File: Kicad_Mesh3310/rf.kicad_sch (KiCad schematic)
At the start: 34 parts, among them U1 TPE4259-63, U10 SX1262IMLTRT, X1 S201632M10PF10PPM 32MHz

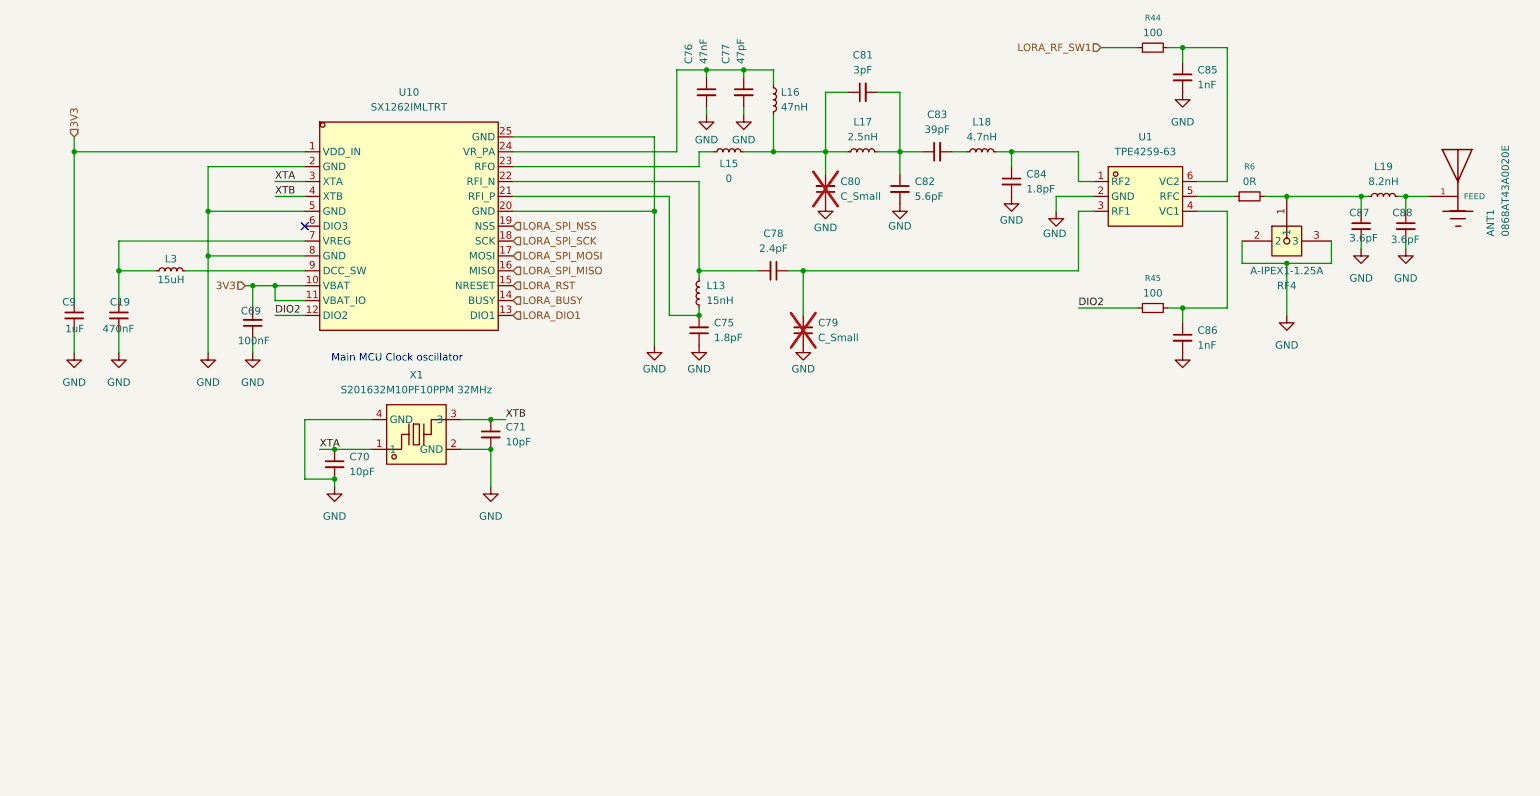
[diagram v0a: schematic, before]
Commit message: shematic changes
small changes in NRF component
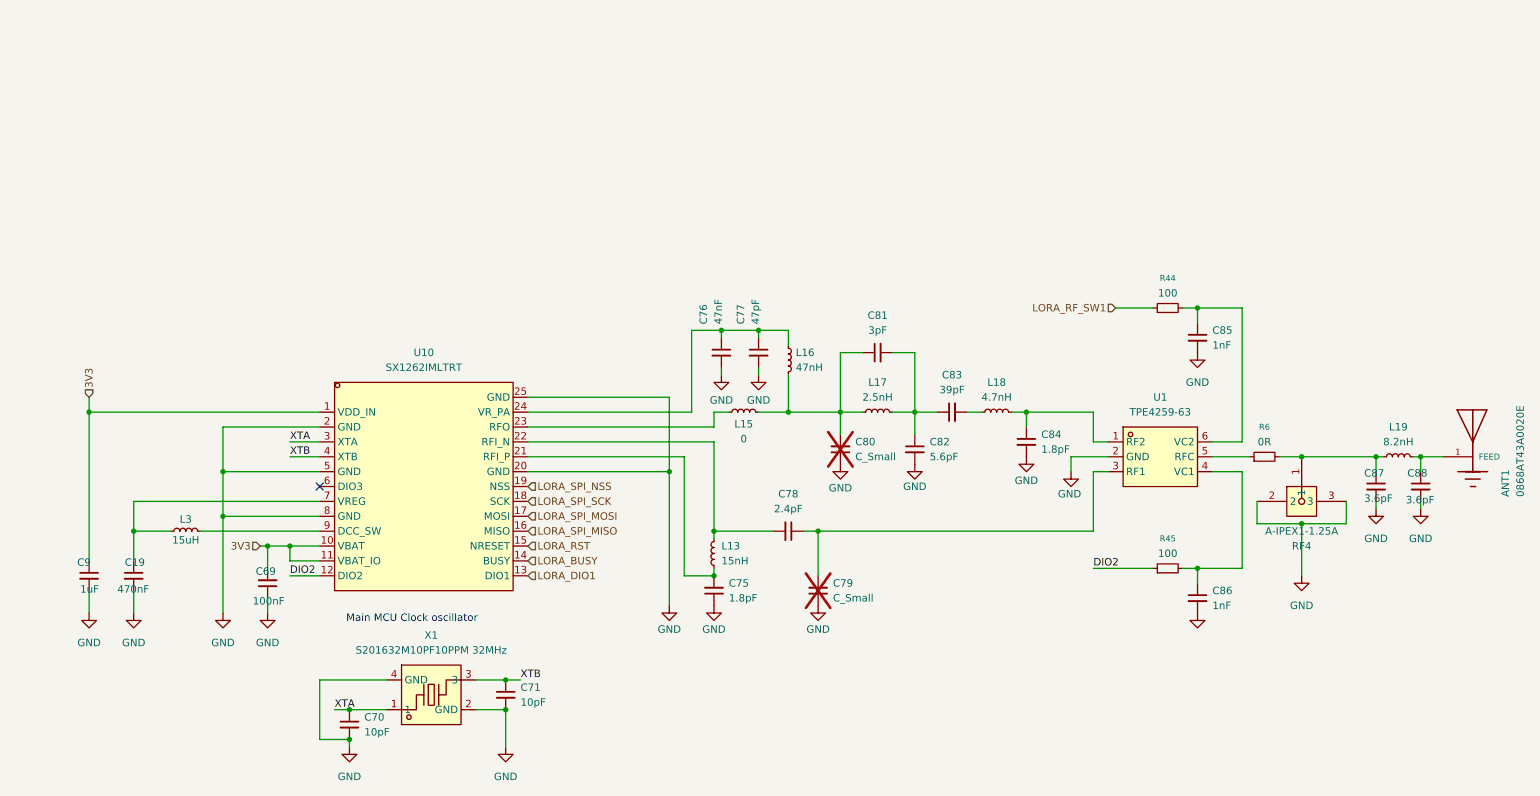
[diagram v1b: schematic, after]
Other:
- moved on the sheet: ANT1, C19, C69, C70, C71, C75, C76, C77, C78, C79, C80, C81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

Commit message: Schematic changes
Adding gsm module , interfaces : mic+earspeaker
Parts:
- C19: footprint Capacitor_SMD:C_0603_1608Metric -> Capacitor_SMD:C_0201_0603Metric
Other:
- note added: "SX1262"
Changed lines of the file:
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@@
 		(comment 1 "JDJ electronics")
 	)
+	(text "SX1262"
+		(exclude_from_sim no)
+		(at 18.542 23.368 0)
+		(effects
+			(font
+				(size 5.08 4.318)
+			)
+			(justify left bottom)
+		)
+	)
 	(text "Main MCU Clock oscillator"
 		(exclude_from_sim no)
@@
 			)
 		)
-		(property "Footprint" "Capacitor_SMD:C_0603_1608Metric"
+		(property "Footprint" "Capacitor_SMD:C_0201_0603Metric"
 			(at 39.37 110.49 0)
 			(effects
